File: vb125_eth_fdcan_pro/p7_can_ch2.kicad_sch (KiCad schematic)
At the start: 1 part, among them J4 D09P33E4GL00LF

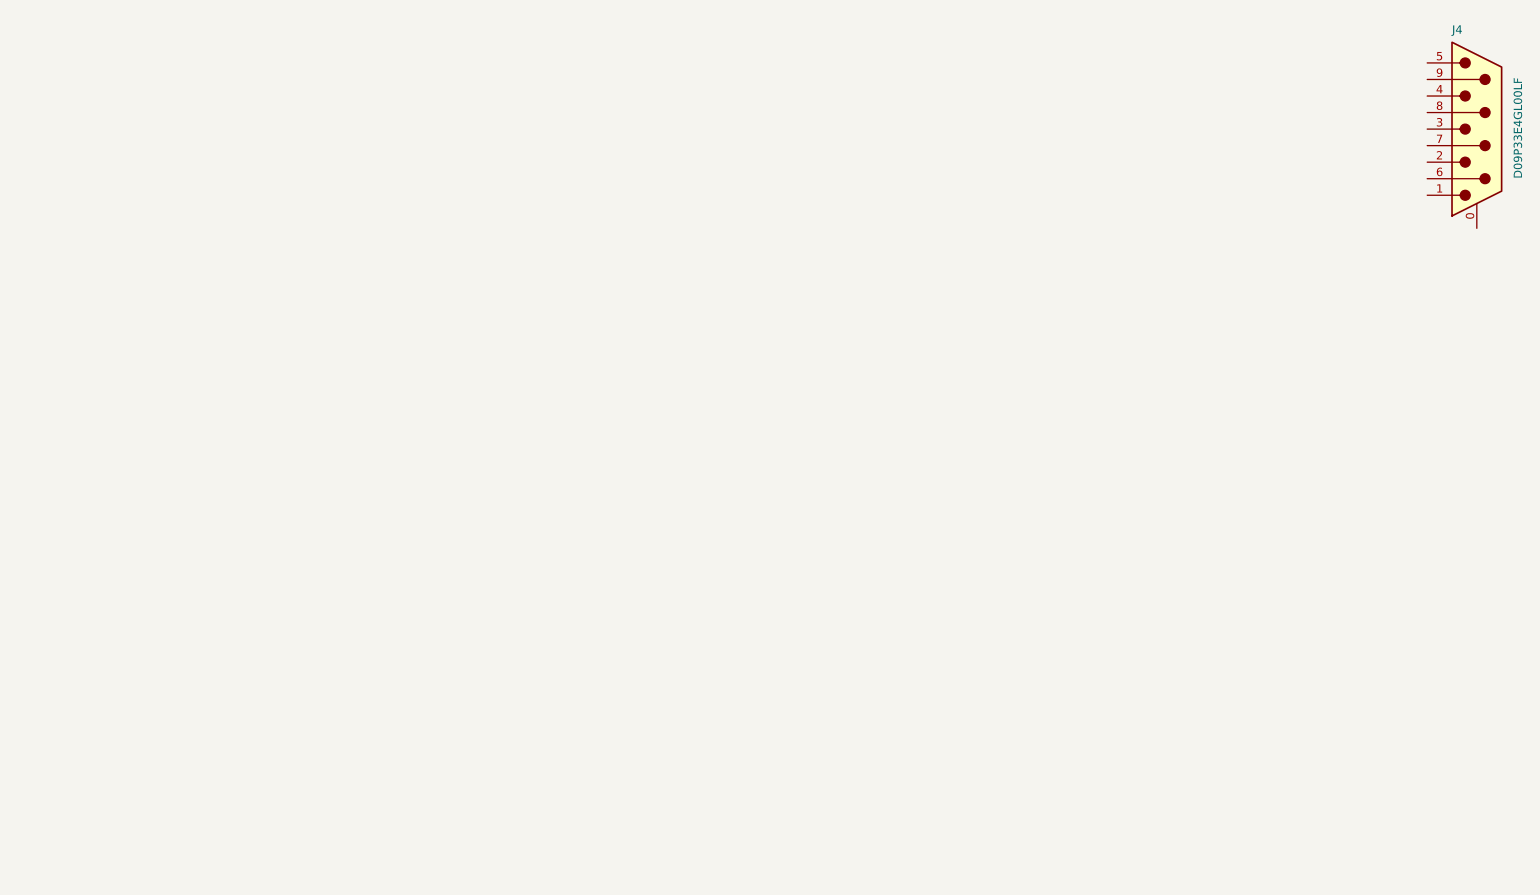
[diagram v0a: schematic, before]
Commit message: CAN schematics. Assign IO on H7.
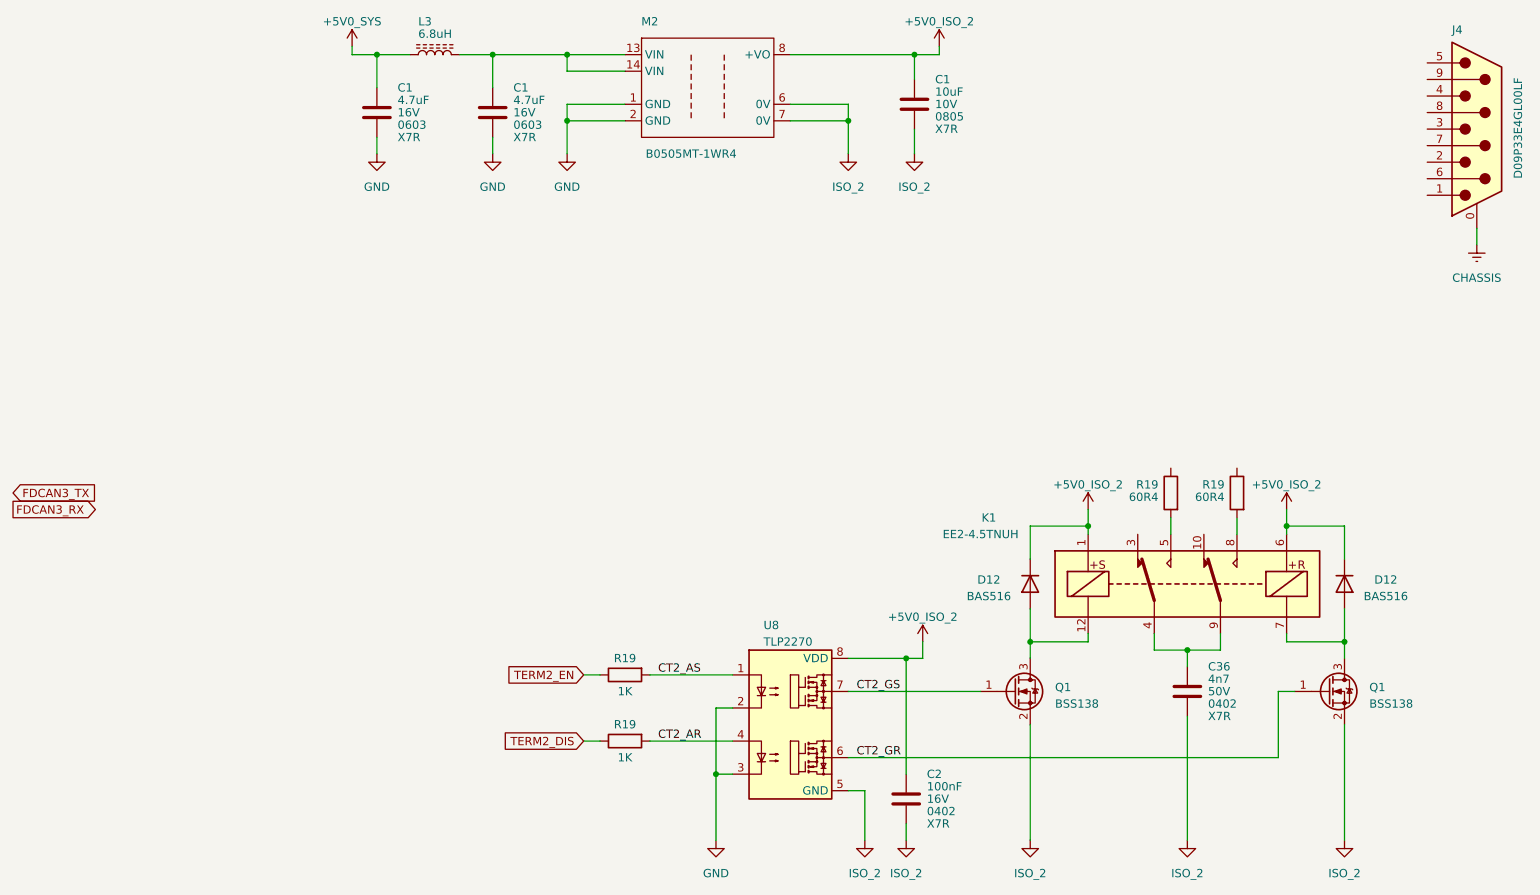
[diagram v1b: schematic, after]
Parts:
- added C1 (x2): 4.7uF, Capacitor_SMD:C_0603_1608Metric, symbol Device:C
- added C1: 10uF, Capacitor_SMD:C_0805_2012Metric, symbol Device:C
- added C2: 100nF, symbol Device:C
- added C36: 4n7, symbol Device:C
- added D12 (x2): BAS516, Diode_SMD:D_SOD-523, symbol Diode:BAS516
- added K1: EE2-4.5TNUH, vhrd_relay:Relay_DPDT_Kemet_EE2_NUH_DoubleCoil, symbol Relay:EE2-4.5TNUH
- added L3: 6.8uH, Inductor_SMD:L_0805_2012Metric, symbol Device:L_Ferrite
- added M2: B0505MT-1WR4, vhrd_module_power:B0505MT-1WR4, symbol vhrd_module_power:B0505MT-1WR4
- added Q1 (x2): BSS138, Package_TO_SOT_SMD:SOT-23, symbol Transistor_FET:BSS138
- added R19 (x2): 60R4, Resistor_SMD:R_0603_1608Metric, symbol Device:R
- added R19 (x2): 1K, Resistor_SMD:R_0402_1005Metric, symbol Device:R
- added U8: TLP2270, vhrd_generic:SO8L_TOS, symbol vhrd_opto_isolators:TLP2270
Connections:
- net CHASSIS: now reaches J4.0 (PAD)
- new net: K1.5, R19.2
- new net: D12.2 (A), K1.12, Q1.3 (D)
- new net: C1.1, L3.2, M2.13 (VIN), M2.14 (VIN)
- new net: C36.1, K1.4, K1.9
- new net: D12.2 (A), K1.7, Q1.3 (D)
- new net: K1.8, R19.2
- new net +5V0_ISO_2: C1.1, C2.1, D12.1 (K), D12.1 (K), K1.1, K1.6, M2.8 (+VO), U8.8 (VDD)
- new net +5V0_SYS: C1.1, L3.1
- new net CT2_AR: R19.2, U8.4
- new net CT2_AS: R19.2, U8.1
- new net CT2_GR: Q1.1 (G), U8.6
- new net CT2_GS: Q1.1 (G), U8.7
- new net GND: C1.2, C1.2, M2.1 (GND), M2.2 (GND), U8.2, U8.3
- new net ISO_2: C1.2, C2.2, C36.2, M2.6 (0V), M2.7 (0V), Q1.2 (S), Q1.2 (S), U8.5 (GND)
- new net TERM2_DIS: R19.1
- new net TERM2_EN: R19.1
